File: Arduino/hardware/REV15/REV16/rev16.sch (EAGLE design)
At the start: 8 parts, among them U1 TC1185SMD

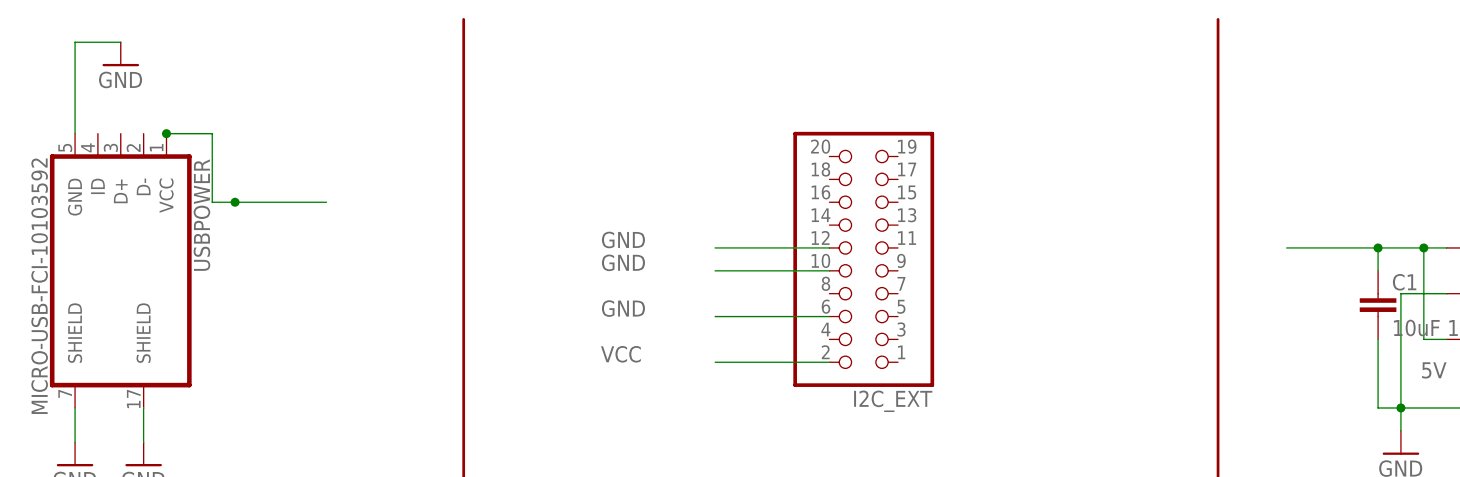
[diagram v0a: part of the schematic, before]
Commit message: up to rev18 DRC check and ground plane
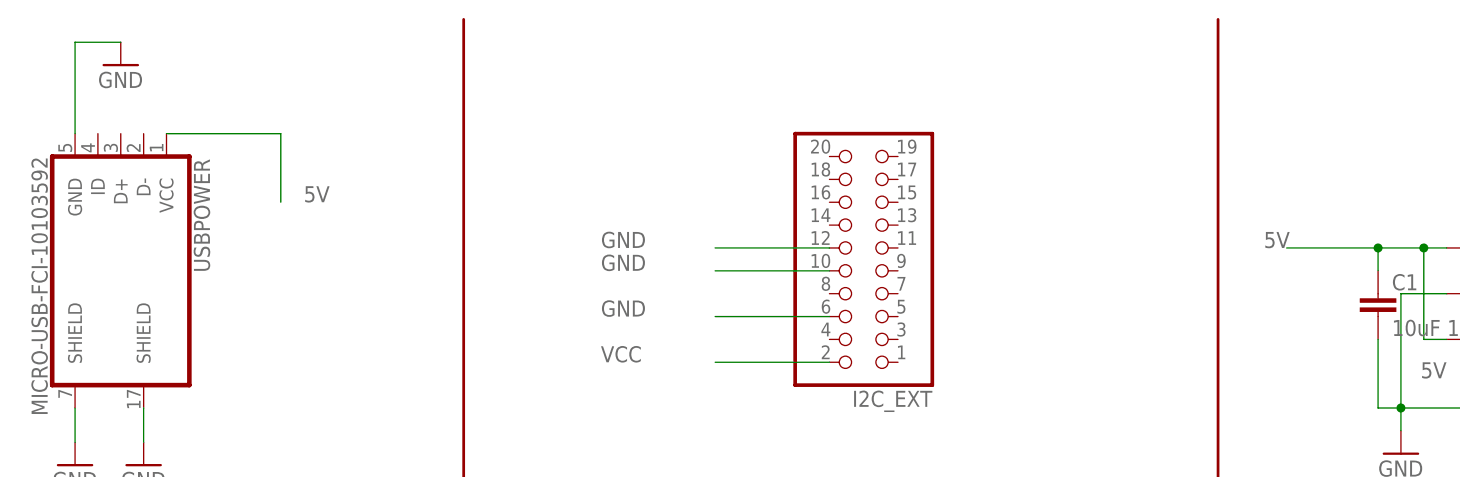
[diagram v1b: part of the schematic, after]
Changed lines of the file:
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@@
 <net name="5V" class="1">
 <segment>
-<wire x1="81.28" y1="243.84" x2="83.82" y2="243.84" width="0.1524" layer="91"/>
-<wire x1="83.82" y1="243.84" x2="93.98" y2="243.84" width="0.1524" layer="91"/>
 <pinref part="USBPOWER" gate="G$1" pin="VCC"/>
-<wire x1="76.2" y1="251.46" x2="81.28" y2="251.46" width="0.1524" layer="91"/>
-<wire x1="81.28" y1="251.46" x2="81.28" y2="243.84" width="0.1524" layer="91"/>
-<junction x="76.2" y="251.46"/>
-<junction x="83.82" y="243.84"/>
+<wire x1="76.2" y1="251.46" x2="88.9" y2="251.46" width="0.1524" layer="91"/>
+<wire x1="88.9" y1="251.46" x2="88.9" y2="243.84" width="0.1524" layer="91"/>
+<label x="91.44" y="243.84" size="1.778" layer="95"/>
 </segment>
 <segment>
@@
 <junction x="210.82" y="238.76"/>
 <wire x1="200.66" y1="238.76" x2="210.82" y2="238.76" width="0.1524" layer="91"/>
+<label x="198.12" y="238.76" size="1.778" layer="95"/>
 </segment>
 </net>

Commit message: REV15-18 cleaned up, need sanity check
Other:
- note added: "Author(s) / Copyright (s): Bo Herrmannsen 2013--2016, Damon Hart-Davis 2013--2016, Mike Stirling 2013"
- note removed: "Author(s) / Copyright (s): Bo Herrmannsen 2013--2014, Damon Hart-Davis 2013--2014, Mike Stirling 2013"
- note removed: "OpenTRV Wireless TRV Controller"
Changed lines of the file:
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@@
 <text x="7.62" y="15.24" size="1.778" layer="91">software, hardware and materials distributed under this Licence</text>
 <text x="7.62" y="12.7" size="1.778" layer="91">is distributed on an "AS IS" BASIS, WITHOUT WARRANTIES OR CONDITIONS</text>
-<text x="7.62" y="2.54" size="1.778" layer="91">Author(s) / Copyright (s): Bo Herrmannsen 2013--2014, Damon Hart-Davis 2013--2014, Mike Stirling 2013</text>
-<text x="289.56" y="33.02" size="1.778" layer="91">OpenTRV Wireless TRV Controller</text>
+<text x="7.62" y="2.54" size="1.778" layer="91">Author(s) / Copyright (s): Bo Herrmannsen 2013--2016, Damon Hart-Davis 2013--2016, Mike Stirling 2013</text>
 <text x="7.62" y="10.16" size="1.778" layer="91"></text>
 <text x="7.62" y="10.16" size="1.778" layer="91">OF ANY KIND, either express or implied. See the Licence for the</text>
